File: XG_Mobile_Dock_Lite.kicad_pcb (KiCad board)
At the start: 4 copper layers, 156.3 x 80.5 mm, 42 parts, among them J1 5-1775443-8, J10 SWD, J11 UART, J12 I2C1, J13 1-1775099-3, J14 3-1775099-2, J17 8730, J2 20455-040E-76, J3 20455-040E-76, J4 3-2362375-4, J5 USB_C_Receptacle, SW1 SW_Push, U12 STM32F030C8Tx

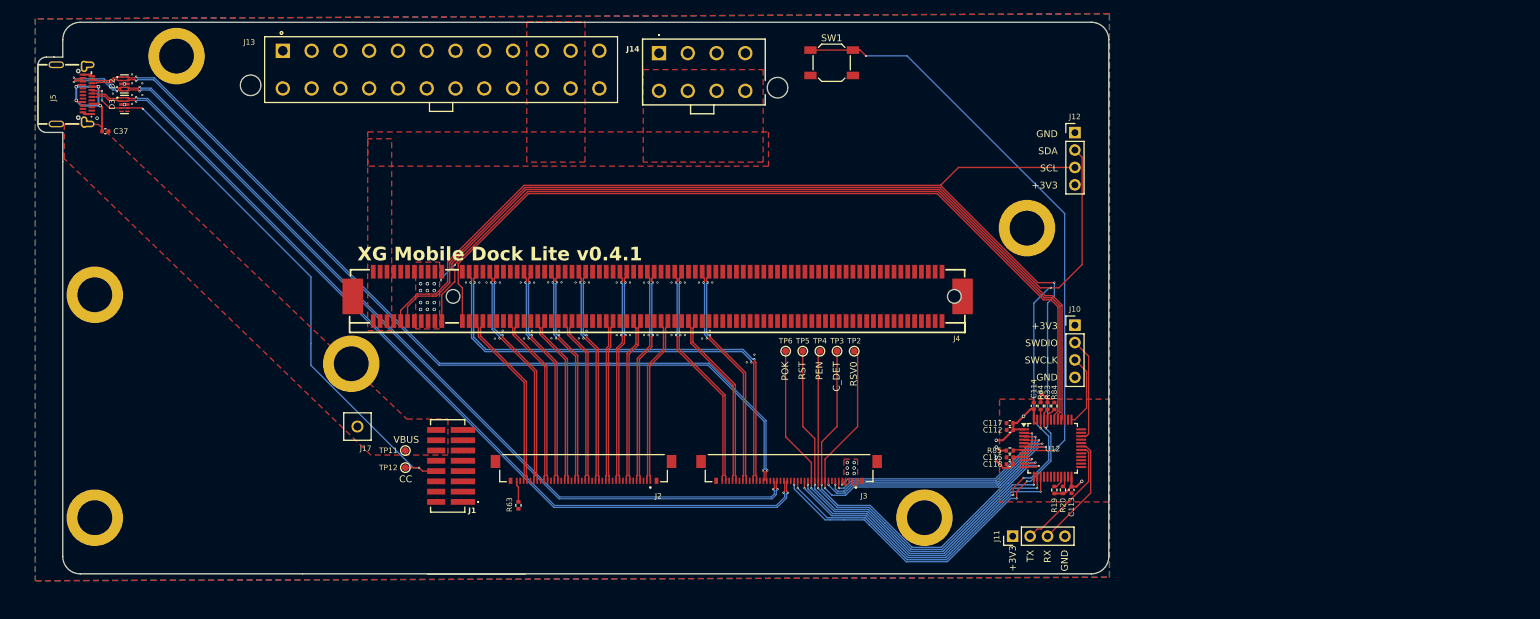
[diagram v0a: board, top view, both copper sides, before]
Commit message: pcb: redesign lite for the ADT-UT3G
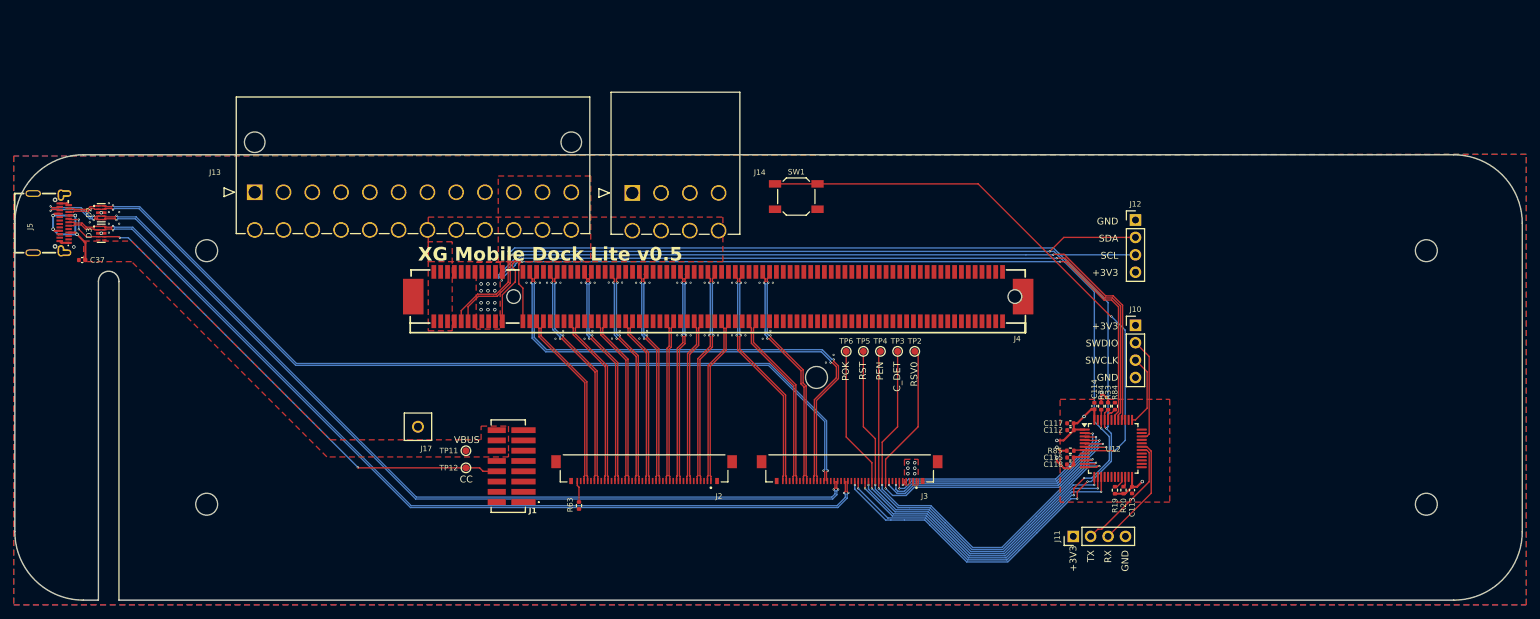
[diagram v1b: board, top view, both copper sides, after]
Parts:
- removed H1, H2, H3, H4, H5, H6: ~, XG_Mobile:Hole_200mil
- added REF**: Hole_3.2mm, XG_Mobile:Hole_3.2mm, F.Cu at (133.8, 71.9)
- added REF**: Hole_3.2mm, XG_Mobile:Hole_3.2mm, F.Cu at (44.8, 53.4)
- added REF**: Hole_3x4mm_Rectangular, XG_Mobile:Hole_3x4mm_Rectangular, F.Cu at (24.0, 98.7)
- added REF**: Hole_3.2mm, XG_Mobile:Hole_3.2mm, F.Cu at (222.8, 90.4)
- added REF**: Hole_3x4mm_Rectangular, XG_Mobile:Hole_3x4mm_Rectangular, F.Cu at (24.0, 58.1)
- added REF**: Hole_3x4mm_Rectangular, XG_Mobile:Hole_3x4mm_Rectangular, F.Cu at (24.0, 78.4)
- added REF**: Hole_3.2mm, XG_Mobile:Hole_3.2mm, F.Cu at (222.8, 53.4)
- added REF**: Hole_3.2mm, XG_Mobile:Hole_3.2mm, F.Cu at (44.8, 90.4)
- J13: value 1-1775099-3 -> 39300240; footprint 1-1775099-3:1-1775099-3 -> 39300240:CON_39300240
- J14: value 3-1775099-2 -> 469911008; footprint 3-1775099-2:317750992 -> 469911008:CON_469911008
- moved J13 32.6 mm to (51.8, 44.9), turned to 180 degrees
- moved J14 20.8 mm to (106.9, 45.0), turned to 180 degrees
- moved SW1 20.2 mm to (130.8, 45.5)
- moved C37 19.1 mm to (26.6, 54.8), turned to 180 degrees
- moved D2 19.1 mm to (29.4, 47.9)
- moved D3 19.1 mm to (29.4, 50.9)
- moved J5 19.1 mm to (22.0, 49.4)
- moved J12 15.5 mm to (180.3, 48.9)
- moved C118 8.84 mm to (170.8, 84.6)
- moved J11 8.84 mm to (171.3, 95.1)
- moved J1 8.84 mm to (88.8, 84.9)
- moved J4 8.84 mm to (119.4, 60.1)
- moved C112 8.84 mm to (170.9, 79.6)
- moved C113 8.84 mm to (179.8, 88.4)
- moved C114 8.84 mm to (174.3, 76.1)
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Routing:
- net /SDA: track 212.7 -> 191.8 mm, vias 5 -> 6
- net /SCL: track 212.4 -> 193.2 mm
- net /CLKREQ#: track 124.2 -> 116.0 mm, vias 0 -> 2
- net /PERST#: track 120.8 -> 112.8 mm
- net /CC: track 83.9 -> 78.8 mm
- net /C_TXP: track 128.8 -> 133.3 mm
- net /C_RXN: track 132.2 -> 136.7 mm
- net /C_RXP: track 131.8 -> 136.2 mm
- net /C_DP: track 129.4 -> 133.8 mm
- net /C_TXN: track 128.4 -> 132.8 mm
- net /C_DN: track 129.8 -> 134.3 mm
- net /CLKP: track 70.2 -> 74.4 mm
- net /CLKN: track 70.2 -> 74.4 mm
- net /RST_SW: track 88.3 -> 84.2 mm
- net /WAKE#: track 126.7 -> 126.6 mm, vias 0 -> 2
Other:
- board size 156.3 x 80.5 mm -> 220 x 65 mm
- board text added: "XG Mobile Dock Lite v0.5"
- board text removed: "XG Mobile Dock Lite v0.4.1"

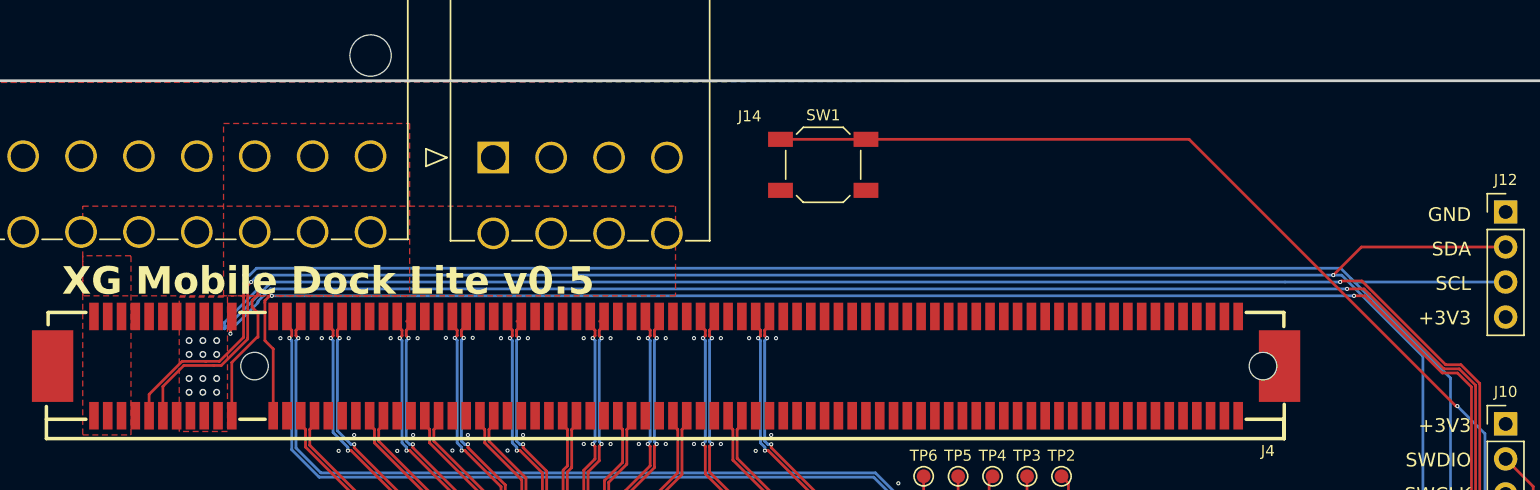
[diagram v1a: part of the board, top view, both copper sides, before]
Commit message: pcb: add 12V pad for external fan connection
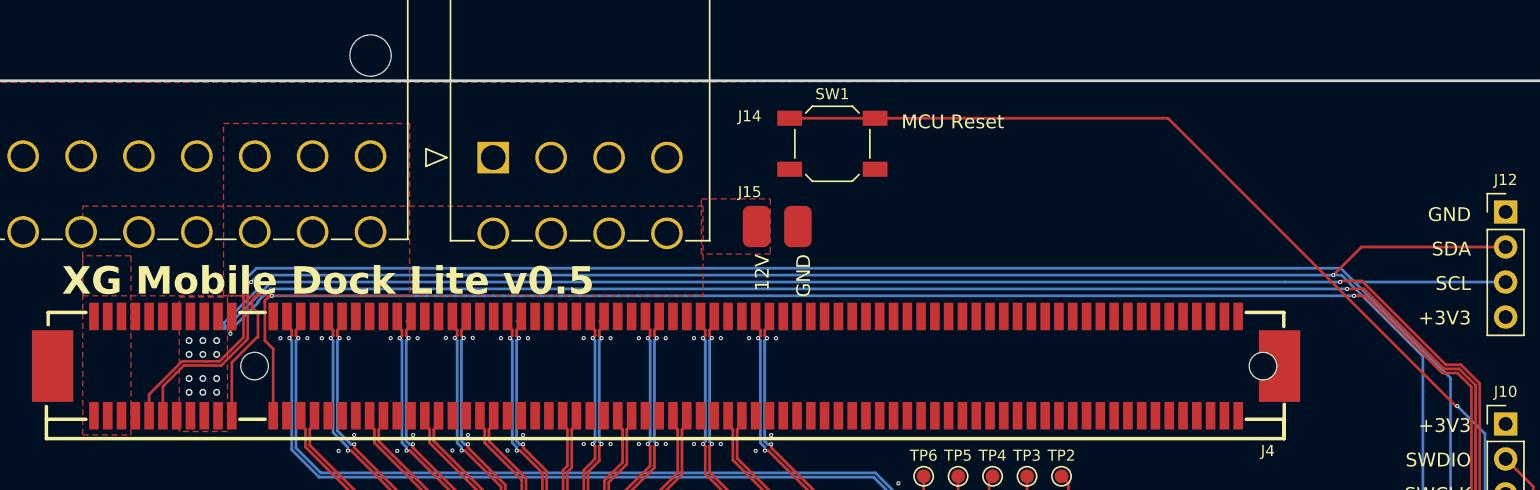
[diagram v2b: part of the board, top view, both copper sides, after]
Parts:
- added J15: Conn_01x02, XG_Mobile:Solder_Pad_2P, F.Cu at (127.5, 50.0)
- moved SW1 1.67 mm to (131.5, 44.0)
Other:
- board text added: "12V"
- board text added: "MCU Reset"
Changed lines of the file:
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@@
 			)
 		)
+		(sheetname "Root")
+		(sheetfile "XG_Mobile_Dock_Lite.kicad_sch")
 		(attr through_hole)
 		(fp_line
@@
 	(footprint "Button_Switch_SMD:SW_SPST_SKQG_WithStem"
 		(layer "F.Cu")
-		(at 130.83666 45.529018)
+		(at 131.5 44)
 		(descr "ALPS 5.2mm Square Low-profile Type (Surface Mount) SKQG Series, With stem, http://www.alps.com/prod/info/E/HTML/Tact/SurfaceMount/SKQG/SKQGAFE010.html")
 		(tags "SPST Button Switch")
@@
 			(polygon
 				(pts
-					(xy 126.83666 44.229018) (xy 129.83666 44.229018) (xy 129.83666 46.829018) (xy 126.83666 46.829018)
+					(xy 127.5 42.7) (xy 130.5 42.7) (xy 130.5 45.3) (xy 127.5 45.3)
 				)
 			)
@@
 			(polygon
 				(pts
-					(xy 131.83666 44.229018) (xy 134.83666 44.229018) (xy 134.83666 46.829018) (xy 131.83666 46.829018)
+					(xy 132.5 42.7) (xy 135.5 42.7) (xy 135.5 45.3) (xy 132.5 45.3)
 				)
 			)
@@
 		)
 	)
+	(footprint "XG_Mobile:Solder_Pad_2P"
+		(layer "F.Cu")
+		(at 127.5 50)
+		(property "Reference" "J15"
+			(at -2 -2.5 0)
+			(unlocked yes)
+			(layer "F.SilkS")
+			(effects
+				(font
+					(size 0.8 0.8)
+					(thickness 0.1)
+				)
+			)
+		)
+		(property "Value" "Conn_01x02"
+			(at 0 2.5 0)
+			(unlocked yes)
+			(layer "F.Fab")
+			(effects
+				(font
+					(size 1 1)
+					(thickness 0.15)
+				)
+			)
+		)
+		(property "Footprint" "XG_Mobile:Solder_Pad_2P"
+			(at 0 0 0)
+			(unlocked yes)
+			(layer "F.Fab")
+			(hide yes)
+			(effects
+				(font
+					(size 1 1)
+					(thickness 0.15)
+				)
+			)
+		)
+		(property "Datasheet" ""
+			(at 0 0 0)
+			(unlocked yes)
+			(layer "F.Fab")
+			(hide yes)
+			(effects
+				(font
+					(size 1 1)
+					(thickness 0.15)
+				)
+			)
+		)
+		(property "Description" "Generic connector, single row, 01x02, script generated (kicad-library-utils/schlib/autogen/connector/)"
+			(at 0 0 0)
+			(unlocked yes)
+			(layer "F.Fab")
+			(hide yes)
+			(effects
+				(font
+					(size 1 1)
+					(thickness 0.15)
+				)
+			)
+		)
+		(property ki_fp_filters "Connector*:*_1x??_*")
+		(sheetname "Root")
+		(sheetfile "XG_Mobile_Dock_Lite.kicad_sch")
+		(attr smd exclude_from_bom)
+		(fp_text user "${REFERENCE}"
+			(at 0 4 0)
+			(unlocked yes)
+			(layer "F.Fab")
+			(effects
+				(font
+					(size 1 1)
+					(thickness 0.15)
+				)
+			)
+		)
+		(pad "1" smd roundrect
+			(at -1.5 0 270)
+			(size 3 2)
+			(layers "F.Cu" "F.Paste" "F.Mask")
+			(roundrect_rratio 0.25)
+			(net 120 "+12V")
+			(pinfunction "Pin_1")
+			(pintype "passive")
+			(thermal_bridge_angle 45)
+		)
+		(pad "2" smd roundrect
+			(at 1.5 0 270)
+			(size 3 2)
+			(layers "F.Cu" "F.Paste" "F.Mask")
+			(roundrect_rratio 0.25)
+			(net 1 "GND")
+			(pinfunction "Pin_2")
+			(pintype "passive")
+			(thermal_bridge_angle 45)
+		)
+	)
 	(footprint "XG_Mobile:Hole_3.2mm"
 		(layer "F.Cu")
@@
 		)
 	)
+	(gr_text "GND"
+		(at 130 52 90)
+		(layer "F.SilkS")
+		(effects
+			(font
+				(size 1 1)
+				(thickness 0.1)
+			)
+			(justify right bottom)
+		)
+	)
 	(gr_text "VBUS"
 		(at 84.621496 81.621496 0)
@@
 		)
 	)
+	(gr_text "MCU Reset"
+		(at 136.5 43 0)
+		(layer "F.SilkS")
+		(effects
+			(font
+				(size 1 1)
+				(thickness 0.1)
+			)
+			(justify left bottom)
+		)
+	)
+	(gr_text "12V"
+		(at 127 52 90)
+		(layer "F.SilkS")
+		(effects
+			(font
+				(size 1 1)
+				(thickness 0.1)
+			)
+			(justify right bottom)
+		)
+	)
 	(gr_text "PEN"
 		(at 143.621496 69.621496 90)
@@
 	)
 	(segment
-		(start 157.379962 43.679018)
-		(end 176.729962 63.029018)
+		(start 173.01166 82.621496)
+		(end 172.92416 82.533996)
 		(width 0.2)
 		(layer "F.Cu")
@@
 	)
 	(segment
-		(start 133.93666 43.679018)
-		(end 157.379962 43.679018)
+		(start 134.6 42.15)
+		(end 155.850944 42.15)
 		(width 0.2)
 		(layer "F.Cu")
@@
 	)
 	(segment
-		(start 173.01166 82.621496)
-		(end 172.92416 82.533996)
+		(start 176.729962 63.029018)
+		(end 176.83666 63.029018)
 		(width 0.2)
 		(layer "F.Cu")
@@
 	)
 	(segment
-		(start 127.73666 43.679018)
-		(end 133.93666 43.679018)
+		(start 177.33666 82.621496)
+		(end 173.01166 82.621496)
 		(width 0.2)
 		(layer "F.Cu")
@@
 	)
 	(segment
-		(start 177.33666 82.621496)
-		(end 173.01166 82.621496)
+		(start 155.850944 42.15)
+		(end 176.729962 63.029018)
 		(width 0.2)
 		(layer "F.Cu")
@@
 	)
 	(segment
-		(start 176.729962 63.029018)
-		(end 176.83666 63.029018)
+		(start 128.4 42.15)
+		(end 134.6 42.15)
 		(width 0.2)
 		(layer "F.Cu")
@@
 	)
 	(zone
+		(net 120)
+		(net_name "+12V")
+		(layer "F.Cu")
+		(hatch edge 0.5)
+		(priority 6)
+		(connect_pads
+			(clearance 0)
+		)
+		(min_thickness 0.25)
+		(filled_areas_thickness no)
+		(fill yes
+			(thermal_gap 0.5)
+			(thermal_bridge_width 0.5)
+		)
+		(polygon
+			(pts
+				(xy 127 48) (xy 127 52) (xy 122 52) (xy 122 48)
+			)
+		)
+	)
+	(zone
 		(net 149)
 		(net_name "/VBUS")
@@
 		(polygon
 			(pts
-				(xy 120.121496 48.529018) (xy 120.121496 55.029018) (xy 77.121496 55.029018) (xy 77.121496 48.529018)
+				(xy 122.121496 48.529018) (xy 122.121496 55.029018) (xy 77.121496 55.029018) (xy 77.121496 48.529018)
 			)
 		)

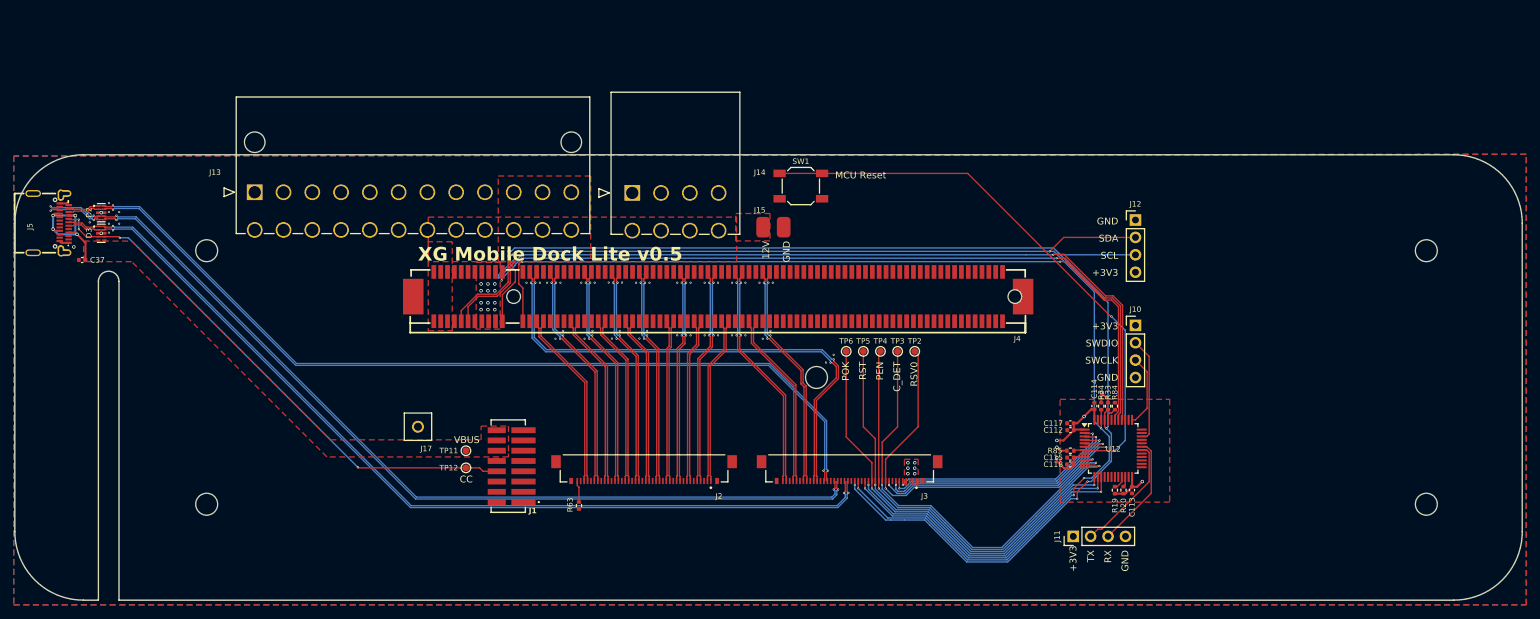
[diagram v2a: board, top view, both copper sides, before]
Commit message: pcb: use 0.3/0.4 vias for reduced cost on lite design
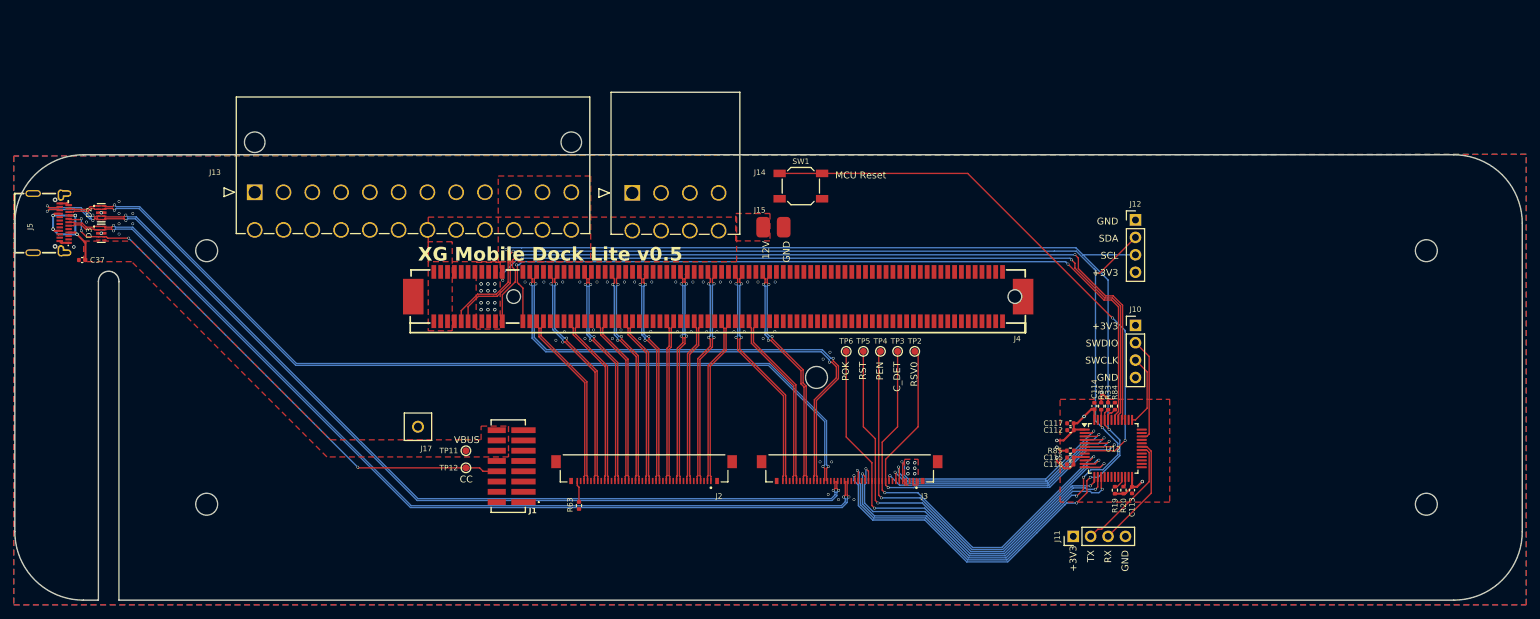
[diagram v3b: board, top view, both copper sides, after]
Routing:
- net /WAKE#: track 126.6 -> 120.0 mm
- net /AC_LOSS: track 44.4 -> 50.1 mm
- net /MCU_IRQ#: track 45.9 -> 50.0 mm
- net /LOCK_SW: track 33.3 -> 37.1 mm
- net /SCL: track 193.2 -> 196.7 mm
- net /SDA: track 191.8 -> 194.8 mm
- net /LED_WHITE#: track 35.0 -> 37.6 mm
- net /RST#: track 64.7 -> 67.3 mm
- net /LED_RED#: track 36.4 -> 38.2 mm
- net /LOCK_DET: track 38.0 -> 39.8 mm
- net /PWREN#: track 62.4 -> 64.1 mm
- net /C_RXP: track 136.2 -> 137.7 mm
- net /C_RXN: track 136.7 -> 138.1 mm
- net /RSV0: track 60.9 -> 62.2 mm
- net /PWROK: track 63.3 -> 64.5 mm
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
